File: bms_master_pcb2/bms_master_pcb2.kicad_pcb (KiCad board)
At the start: 4 copper layers, 100 x 80 mm, 111 parts, among them J101 EXTRA COMMS, J102 GPIO, J103 EXTRA POWER, J104 TC2030, J105 EXTRA BMS OUTPUTS, J106 OUT, J201 Conn_01x04, J202 Conn_01x04, J301 USB4085-GF-A, U101 STM32G474RETx, U102 SST26VF064B-104V/MF, U201 LTC6820HMS-TRPBF, U202 LTC6820HMS-TRPBF, U301 USBLC6-2SC6, U401 TCAN1044AVDDFRQ1, U402 TCAN1044AVDDFRQ1, U502 AP2112K-3.3, U503 LMR33620CQ5RNXRQ1, U601 TPL7407LAD

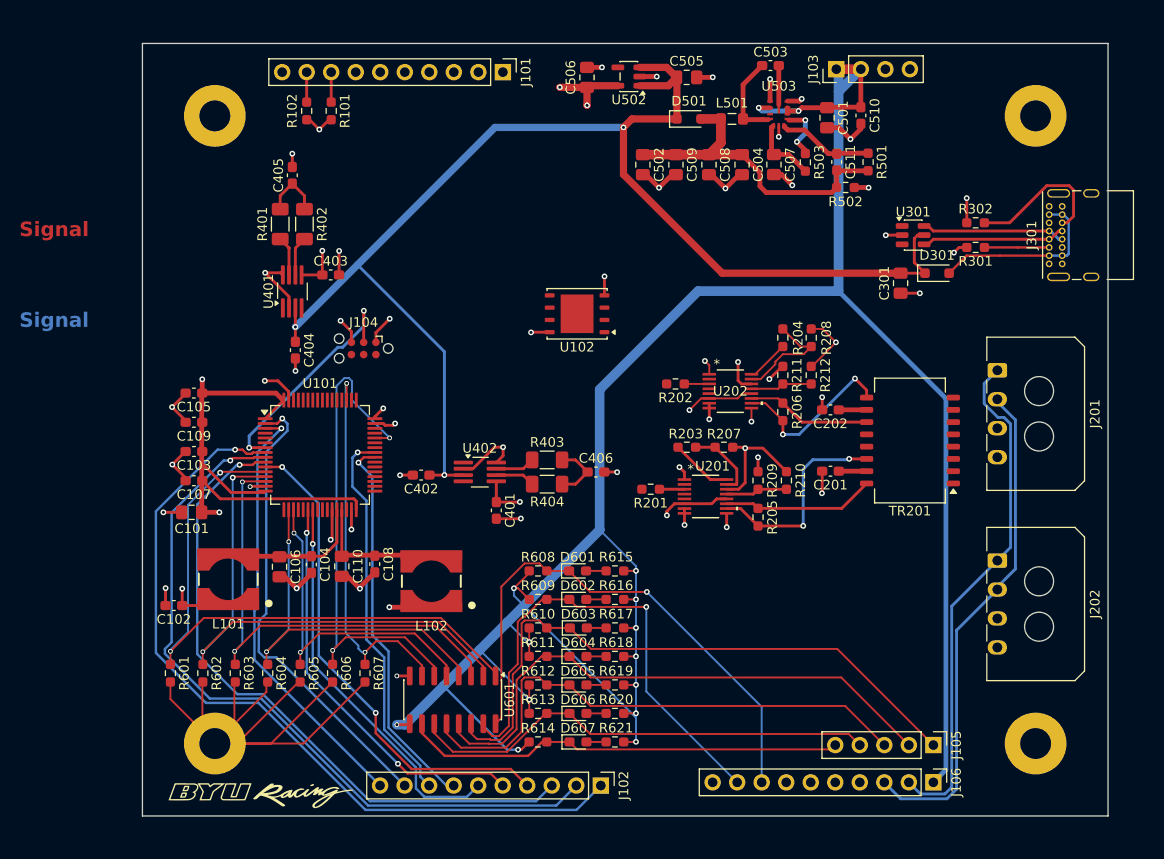
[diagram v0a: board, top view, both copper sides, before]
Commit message: added diff routing for usb
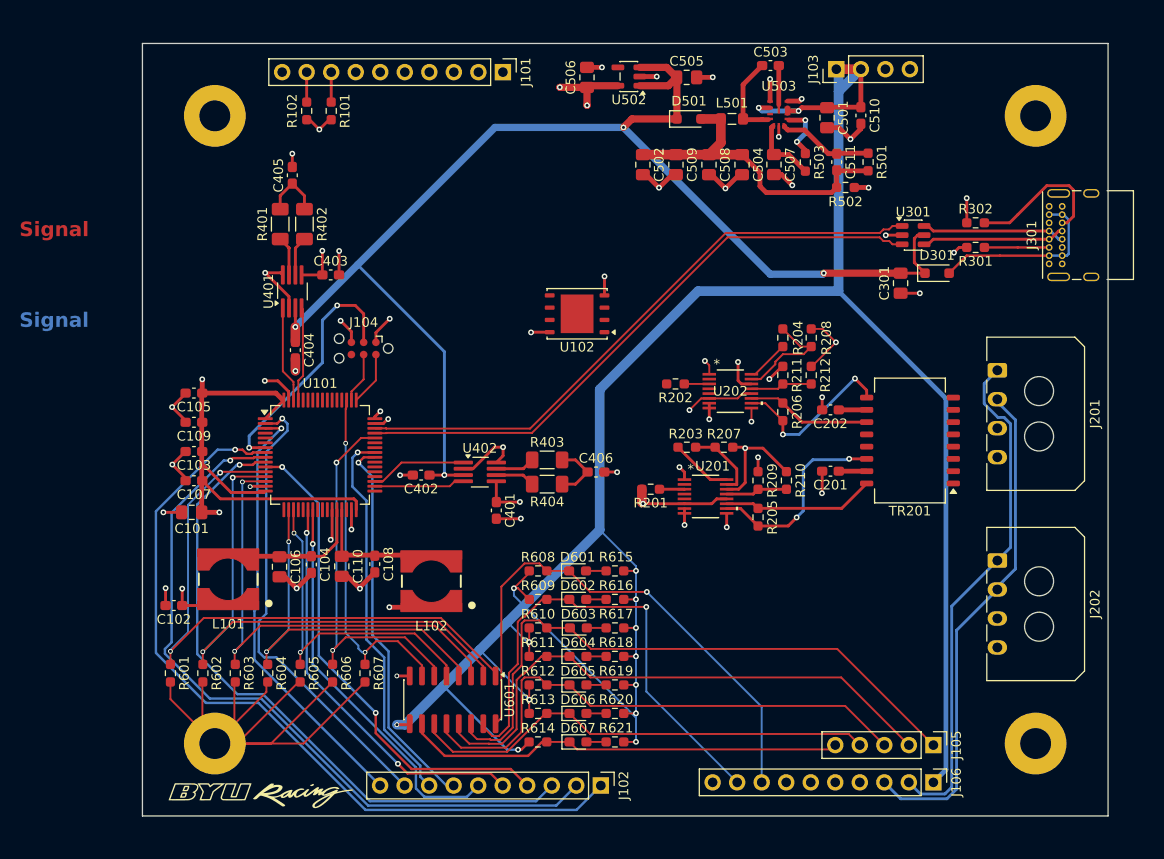
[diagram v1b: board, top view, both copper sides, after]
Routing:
- net /USB/USB.D+: track 0.00 -> 63.3 mm
- net /USB/USB.D-: track 0.00 -> 63.3 mm
- net /DIG_OUT_5: track 53.4 -> 39.4 mm
- net /CAN/CAN1.TX: track 0.00 -> 10.0 mm
- net /CAN/CAN2.TX: track 0.00 -> 9.97 mm
- net /CAN/CAN1.RX: track 0.00 -> 9.81 mm
- net /CAN/CAN2.RX: track 0.00 -> 9.37 mm
- net /SWDIO: track 0.00 -> 5.56 mm
- net /SWCLK: track 0.00 -> 5.24 mm
- net /DIG_OUT_6: track 40.4 -> 36.9 mm
- net +5V: track 139.2 -> 136.4 mm, vias 3 -> 4
- net +3.3V: track 115.3 -> 118.0 mm
- net /RESET: track 24.4 -> 26.2 mm
- net Net-(TR201-TD+): track 21.6 -> 20.6 mm
- net GND: track 204.8 -> 204.1 mm

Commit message: Add files via upload
finished and ready to order V1.01
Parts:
- removed the G*** at (143.1, 125.5)
- added G***: LOGO, LOGO, F.Cu at (201.2, 124.5)
- added G***: LOGO, LOGO, B.Cu at (201.5, 124.5)
- J105: footprint Connector_PinHeader_2.54mm:PinHeader_1x05_P2.54mm_Vertical -> Connector_PinHeader_2.54mm:PinHeader_1x07_P2.54mm_Vertical
- J106: footprint Connector_PinHeader_2.54mm:PinHeader_1x10_P2.54mm_Vertical -> Connector_PinHeader_2.54mm:PinHeader_1x06_P2.54mm_Vertical
- moved J106 98.1 mm to (135.3, 64.2), turned to 0 degrees
- moved C103 21.3 mm to (157.0, 84.7), turned to 0 degrees
- moved C107 20.3 mm to (156.4, 96.3), turned to 0 degrees
- moved C201 12.1 mm to (205.7, 103.5), turned to -90 degrees
- moved TR201 7.35 mm to (210.5, 96.1)
- moved C105 6.46 mm to (142.8, 83.9)
- moved C101 5.72 mm to (141.9, 96.0)
- moved C109 4.49 mm to (140.9, 86.5)
- moved C202 4.48 mm to (205.5, 88.7), turned to 90 degrees
- moved J104 3.28 mm to (157.1, 80.0)
- moved R206 1.47 mm to (198.8, 85.7)
- moved U102 1.44 mm to (174.7, 76.0)
- moved R205 1.42 mm to (196.2, 96.6)
- moved J103 0.85 mm to (202.9, 51.1)
- moved J105 0.70 mm to (212.9, 119.6)
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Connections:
- net /FDCAN3_RX renamed /FDCAN3.D-
- net /FDCAN3_TX renamed /FDCAN3.D+
- J105 pad 1: /Digital Outputs and Happy Lights/BMS_OUT_2 -> /Digital Outputs and Happy Lights/BMS_OUT_0
- J105 pad 2: /Digital Outputs and Happy Lights/BMS_OUT_3 -> /Digital Outputs and Happy Lights/BMS_OUT_1
- J105 pad 3: /Digital Outputs and Happy Lights/BMS_OUT_4 -> /Digital Outputs and Happy Lights/BMS_OUT_2
- J105 pad 4: /Digital Outputs and Happy Lights/BMS_OUT_5 -> /Digital Outputs and Happy Lights/BMS_OUT_3
- J105 pad 5: /Digital Outputs and Happy Lights/BMS_OUT_6 -> /Digital Outputs and Happy Lights/BMS_OUT_4
- J106 pad 2: /isoSPI/E-METER_PASSTHROUGH_1 -> /CAN/CAN.1-
- J106 pad 3: /isoSPI/E-METER_PASSTHROUGH_2 -> /CAN/CAN.1+
- J106 pad 4: /CAN/CAN1.H -> /CAN/CAN.2+
- J106 pad 5: /CAN/CAN1.L -> /CAN/CAN.2-
- J106 pad 6: /CAN/CAN2.H -> GND
- J201 pad 3: Net-(J201-Pin_3) -> /isoSPI/OUTPUT_isoSPI.D+
- J201 pad 4: Net-(J201-Pin_4) -> /isoSPI/OUTPUT_isoSPI.D-
- J202 pad 3: Net-(J202-Pin_3) -> /isoSPI/INPUT_isoSPI.D+
- J202 pad 4: Net-(J202-Pin_4) -> /isoSPI/INPUT_isoSPI.D-
- R205 pad 1: Net-(TR201-TD+) -> /isoSPI/isoSPI.D-
- R205 pad 2: Net-(TR201-TD-) -> /isoSPI/isoSPI.D+
- R206 pad 1: Net-(TR201-RD+) -> /isoSPI/isoSPI_2.D-
- R206 pad 2: Net-(TR201-RD-) -> /isoSPI/isoSPI_2.D+
- R401 pad 1: /CAN/CAN1.H -> /CAN/CAN.1+
- R402 pad 2: /CAN/CAN1.L -> /CAN/CAN.1-
- R403 pad 1: /CAN/CAN2.H -> /CAN/CAN.2+
- R404 pad 2: /CAN/CAN2.L -> /CAN/CAN.2-
- TR201 pad 1: Net-(J202-Pin_3) -> /isoSPI/INPUT_isoSPI.D-
- TR201 pad 11: Net-(TR201-RD-) -> /isoSPI/isoSPI_2.D-
- TR201 pad 14: Net-(TR201-TD+) -> /isoSPI/isoSPI.D+
- TR201 pad 16: Net-(TR201-TD-) -> /isoSPI/isoSPI.D-
- TR201 pad 3: Net-(J202-Pin_4) -> /isoSPI/INPUT_isoSPI.D+
- TR201 pad 6: Net-(J201-Pin_3) -> /isoSPI/OUTPUT_isoSPI.D-
- TR201 pad 8: Net-(J201-Pin_4) -> /isoSPI/OUTPUT_isoSPI.D+
- TR201 pad 9: Net-(TR201-RD+) -> /isoSPI/isoSPI_2.D+
- U102 pad 1: /NCS -> /QSPI.NCS
- U102 pad 2: /IO1 -> /QSPI.IO1
- U102 pad 3: /IO2 -> /QSPI.IO2
- U102 pad 5: /IO0 -> /QSPI.IO0
- U102 pad 6: /CLK -> /QSPI.CLK
- U102 pad 7: /IO3 -> /QSPI.IO3
- U102 pad 9: (no net) -> GND
- U201 pad 10: Net-(TR201-TD+) -> /isoSPI/isoSPI.D-
- U201 pad 11: Net-(TR201-TD-) -> /isoSPI/isoSPI.D+
- U202 pad 10: Net-(TR201-RD+) -> /isoSPI/isoSPI_2.D-
- U202 pad 11: Net-(TR201-RD-) -> /isoSPI/isoSPI_2.D+
- U401 pad 6: /CAN/CAN1.L -> /CAN/CAN.1-
- U401 pad 7: /CAN/CAN1.H -> /CAN/CAN.1+
- U402 pad 6: /CAN/CAN2.L -> /CAN/CAN.2-
- U402 pad 7: /CAN/CAN2.H -> /CAN/CAN.2+
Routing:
- net /isoSPI/SPI2.SCK: track 0.00 -> 102.8 mm, vias 0 -> 4
- net /CAN/CAN.2+: track 0.00 -> 95.5 mm
- net /CAN/CAN.2-: track 0.00 -> 95.4 mm
- net +12V: track 263.1 -> 346.5 mm
- net GND: track 204.1 -> 131.2 mm, vias 44 -> 335
- net /SPI_CS2: track 0.00 -> 57.7 mm, vias 0 -> 2
- net /I2C2_SCL: track 3.10 -> 59.5 mm, vias 0 -> 1
- net /I2C2_SDA: track 3.10 -> 58.2 mm, vias 0 -> 1
- net /QSPI.IO2: track 0.00 -> 52.9 mm, vias 0 -> 2
- net /SPI_CS1: track 0.00 -> 51.3 mm, vias 0 -> 2
- net /isoSPI/SPI2.MOSI: track 0.00 -> 47.1 mm, vias 0 -> 3
- net /QSPI.IO1: track 0.00 -> 45.7 mm, vias 0 -> 2
- net /isoSPI/SPI2.MISO: track 5.17 -> 48.3 mm
- net /QSPI.CLK: track 0.00 -> 40.8 mm, vias 0 -> 2
- net /QSPI.IO0: track 0.00 -> 39.9 mm, vias 0 -> 2
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- added copper zone on B.Cu, net GND
- added copper zone on F.Cu, net GND
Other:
- board text added: "+ -"
- board text added: "+12V CAN1 CAN2 GND L H H L"
- board text added: "+12V | GND"
- board text added: "BMS Master Board 2027 V1.01 Harrison Kirkham Rugby Taylor Ryan Huber"
- board text added: "BMS OUTPUTS: 6 5 4 3 2 1 0"
- board text added: "GND I2C I2C FD FD UART |--SPI3-|3.3V"
- board text added: "GPIOs: 9 8 7 6 5 4 3 2 1 0"
- board text removed: "GND"
- board text removed: "PWR"
- board text removed: "Signal"
